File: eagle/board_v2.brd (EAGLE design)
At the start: 104.4 x 80.6 mm, 35 parts, among them J1 RJ11-4X, J2 RJ11-4X, Q1 BD140, Q10 BD140, Q11 BD140, Q12 BD140, Q13 BD140, Q14 BD140, Q15 BD140, Q2 BD140, Q3 BD140, Q4 BD140, Q5 BD140, Q6 BD140, Q7 BD140, Q8 BD140, Q9 BD140, X1 RJ45-8X, X2 RJ45-8X, X3 RJ45-8X, X4 RJ45-8X, X5 RJ45-8X, X6 RJ45-8X

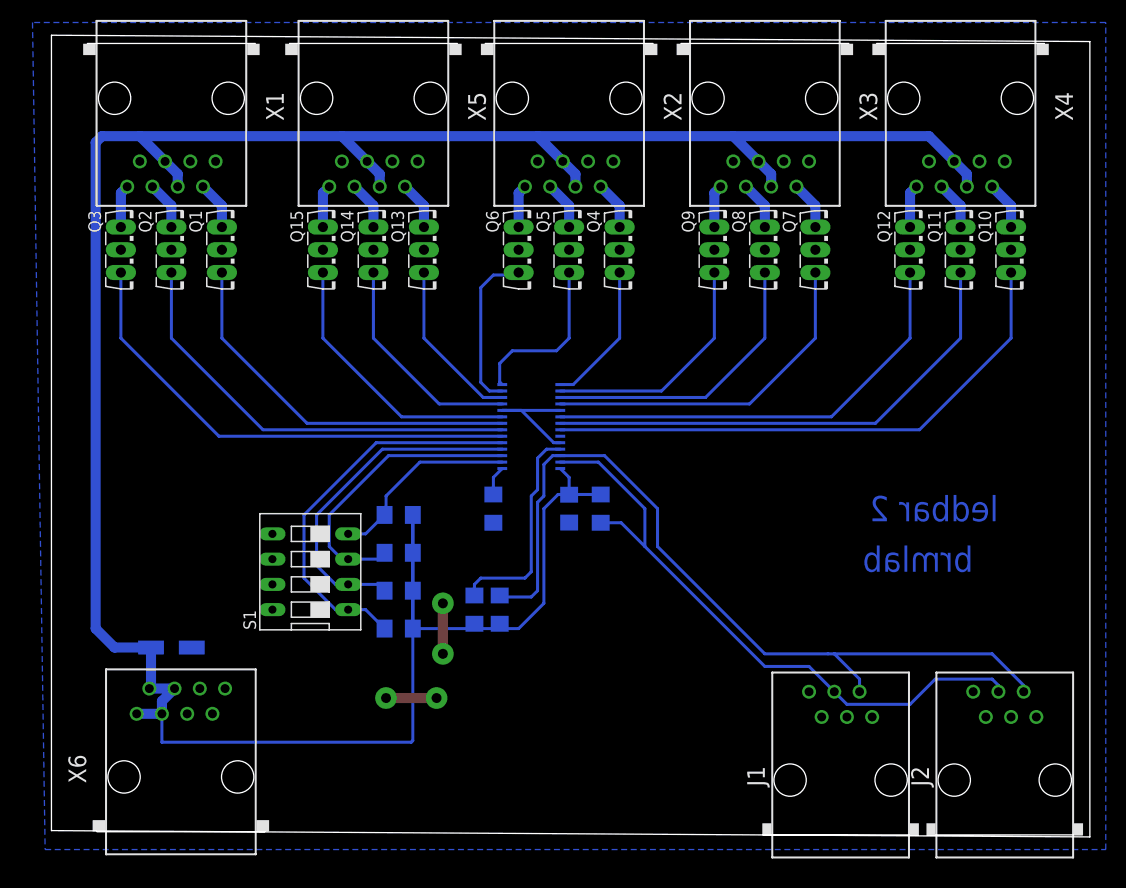
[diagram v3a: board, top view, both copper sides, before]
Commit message: i2c in crossover; removed jumper wires
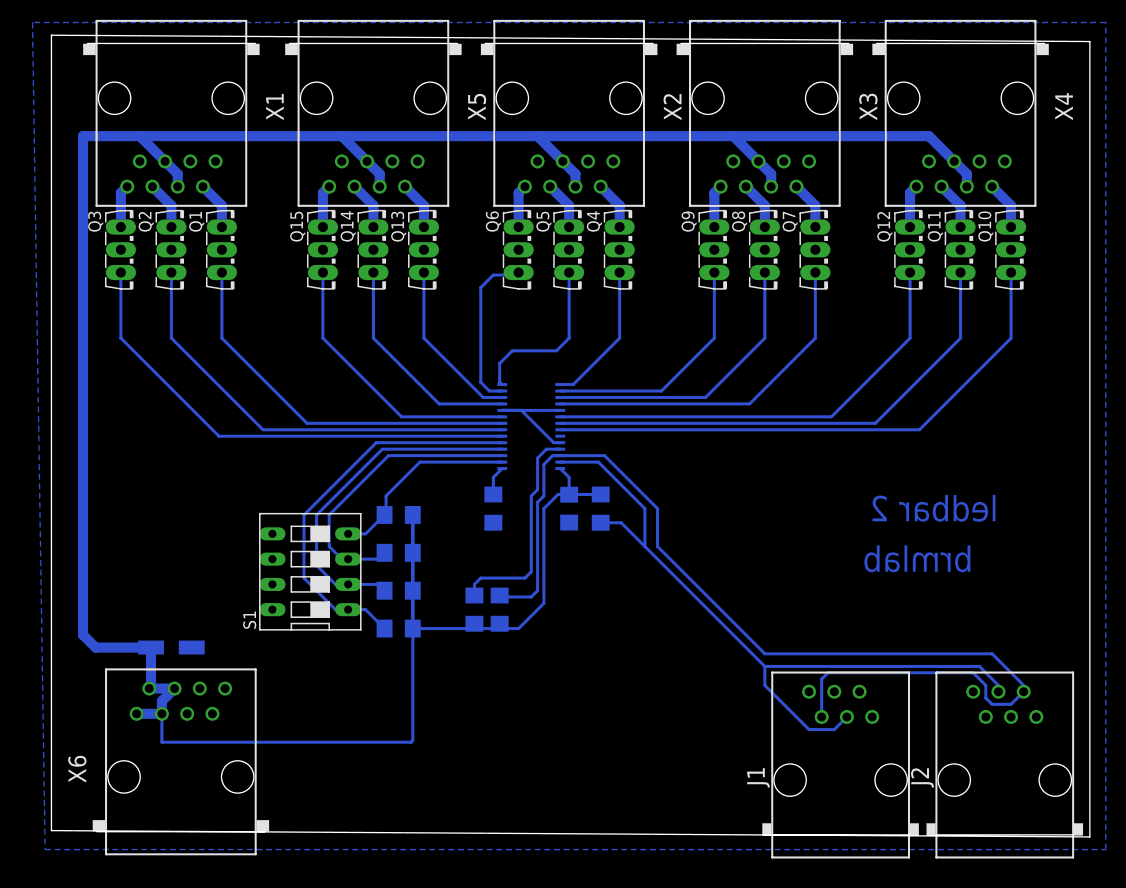
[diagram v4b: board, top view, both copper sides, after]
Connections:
- net GND: now also J1.3, J1.5; no longer J1.2, J1.4
- net N$37: now also J1.2; no longer J1.5
- net N$38: now also J1.4; no longer J1.3
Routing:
- net N$37: track 83.0 -> 105.1 mm
- net N$38: track 63.8 -> 74.2 mm
- net GND: track 23.2 -> 13.0 mm, vias 4 -> 0
- net +5V: track 284.5 -> 287.8 mm
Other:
- board text added: "C1"
- board text added: "C2"
- board text added: "J1"
- board text added: "J2"
- board text added: "Q1"
- board text added: "Q10"
- board text added: "Q11"
- board text added: "Q12"
- board text added: "Q13"
- board text added: "Q14"
- board text added: "Q15"
- board text added: "Q2"
- board text added: "Q3"
- board text added: "Q4"
- board text added: "Q5"
- board text added: "Q6"
- board text added: "Q7"
- board text added: "Q8"
- board text added: "Q9"
- board text added: "R1"
- board text added: "R2"
- board text added: "R3"
- board text added: "R4"
- board text added: "R5"
- board text added: "R6"
- board text added: "R7"
- board text added: "R8"
- board text added: "S1"
- board text added: "U$1"
- board text added: "X1"
- board text added: "X2"
- board text added: "X3"
- board text added: "X4"
- board text added: "X5"
- board text added: "X6"
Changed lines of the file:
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@@
 <layer number="97" name="Info" color="7" fill="1" visible="no" active="no"/>
 <layer number="98" name="Guide" color="6" fill="1" visible="no" active="no"/>
+<layer number="125" name="_tNames" color="14" fill="1" visible="yes" active="yes"/>
+<layer number="126" name="_bNames" color="5" fill="1" visible="yes" active="yes"/>
 <layer number="250" name="Descript" color="3" fill="1" visible="no" active="no"/>
 <layer number="251" name="SMDround" color="12" fill="11" visible="no" active="no"/>
@@
 <text x="95.25" y="31.115" size="2.54" layer="16" font="vector" rot="MR0">ledbar 2</text>
 <text x="92.71" y="26.035" size="2.54" layer="16" font="vector" rot="MR0">brmlab</text>
+<text x="50.927" y="33.655" size="1.27" layer="126" rot="MR270">C1</text>
+<text x="14.66499375" y="21.16500625" size="1.016" layer="126" rot="MR0">C2</text>
+<text x="71.755" y="4.445" size="1.778" layer="125" rot="R90">J1</text>
+<text x="88.265" y="4.445" size="1.778" layer="125" rot="R90">J2</text>
+<text x="13.8684" y="62.3824" size="1.27" layer="125" ratio="10" rot="R270">Q1</text>
+<text x="8.7884" y="62.3824" size="1.27" layer="125" ratio="10" rot="R270">Q2</text>
+<text x="3.7084" y="62.3824" size="1.27" layer="125" ratio="10" rot="R270">Q3</text>
+<text x="53.8734" y="62.3824" size="1.27" layer="125" ratio="10" rot="R270">Q4</text>
+<text x="48.7934" y="62.3824" size="1.27" layer="125" ratio="10" rot="R270">Q5</text>
+<text x="43.7134" y="62.3824" size="1.27" layer="125" ratio="10" rot="R270">Q6</text>
+<text x="73.5584" y="62.3824" size="1.27" layer="125" ratio="10" rot="R270">Q7</text>
+<text x="68.4784" y="62.3824" size="1.27" layer="125" ratio="10" rot="R270">Q8</text>
+<text x="63.3984" y="62.3824" size="1.27" layer="125" ratio="10" rot="R270">Q9</text>
+<text x="93.2434" y="62.3824" size="1.27" layer="125" ratio="10" rot="R270">Q10</text>
+<text x="88.1634" y="62.3824" size="1.27" layer="125" ratio="10" rot="R270">Q11</text>
+<text x="83.0834" y="62.3824" size="1.27" layer="125" ratio="10" rot="R270">Q12</text>
+<text x="34.1884" y="62.3824" size="1.27" layer="125" ratio="10" rot="R270">Q13</text>
+<text x="29.1084" y="62.3824" size="1.27" layer="125" ratio="10" rot="R270">Q14</text>
+<text x="24.0284" y="62.3824" size="1.27" layer="125" ratio="10" rot="R270">Q15</text>
+<text x="45.593" y="30.988" size="1.27" layer="126" rot="MR90">R1</text>
+<text x="43.942" y="23.622" size="1.27" layer="126" rot="MR270">R2</text>
+<text x="56.388" y="30.988" size="1.27" layer="126" rot="MR90">R3</text>
+<text x="41.402" y="23.622" size="1.27" layer="126" rot="MR270">R4</text>
+<text x="36.322" y="21.463" size="1.27" layer="126" rot="MR0">R5</text>
+<text x="36.322" y="25.273" size="1.27" layer="126" rot="MR0">R6</text>
+<text x="36.322" y="29.083" size="1.27" layer="126" rot="MR0">R7</text>
+<text x="36.322" y="32.893" size="1.27" layer="126" rot="MR0">R8</text>
+<text x="20.574" y="20.193" size="1.27" layer="125" ratio="10" rot="R90">S1</text>
+<text x="46.1772" y="35.469396875" size="1.016" layer="126" ratio="10" rot="MR180">U$1</text>
+<text x="21.59" y="74.295" size="1.778" layer="125" rot="R270">X1</text>
+<text x="61.595" y="74.295" size="1.778" layer="125" rot="R270">X2</text>
+<text x="81.28" y="74.295" size="1.778" layer="125" rot="R270">X3</text>
+<text x="100.965" y="74.295" size="1.778" layer="125" rot="R270">X4</text>
+<text x="41.91" y="74.295" size="1.778" layer="125" rot="R270">X5</text>
+<text x="3.4925" y="4.7625" size="1.778" layer="125" rot="R90">X6</text>
 </plain>
 <attributes>
@@
 <param name="mtCopper" value="0.035mm 0.035mm 0.035mm 0.035mm 0.035mm 0.035mm 0.035mm 0.035mm 0.035mm 0.035mm 0.035mm 0.035mm 0.035mm 0.035mm 0.035mm 0.035mm"/>
 <param name="mtIsolate" value="1.5mm 0.15mm 0.2mm 0.15mm 0.2mm 0.15mm 0.2mm 0.15mm 0.2mm 0.15mm 0.2mm 0.15mm 0.2mm 0.15mm 0.2mm"/>
-<param name="mdWireWire" value="16mil"/>
+<param name="mdWireWire" value="20mil"/>
 <param name="mdWirePad" value="20mil"/>
-<param name="mdWireVia" value="16mil"/>
-<param name="mdPadPad" value="16mil"/>
-<param name="mdPadVia" value="16mil"/>
-<param name="mdViaVia" value="16mil"/>
+<param name="mdWireVia" value="20mil"/>
+<param name="mdPadPad" value="20mil"/>
+<param name="mdPadVia" value="20mil"/>
+<param name="mdViaVia" value="20mil"/>
 <param name="mdSmdPad" value="0mil"/>
 <param name="mdSmdVia" value="0mil"/>
@@
 <wire x1="48.895" y1="69.85" x2="29.21" y2="69.85" width="1.016" layer="16"/>
 <wire x1="29.21" y1="69.85" x2="8.89" y2="69.85" width="1.016" layer="16"/>
-<wire x1="8.89" y1="69.85" x2="5.08" y2="69.85" width="1.016" layer="16"/>
-<wire x1="5.08" y1="69.85" x2="4.445" y2="69.215" width="1.016" layer="16"/>
-<wire x1="4.445" y1="69.215" x2="4.445" y2="20.32" width="1.016" layer="16"/>
-<wire x1="4.445" y1="20.32" x2="6.35" y2="18.415" width="1.016" layer="16"/>
-<wire x1="6.35" y1="18.415" x2="10.015" y2="18.415" width="1.016" layer="16"/>
+<wire x1="8.89" y1="69.85" x2="3.175" y2="69.85" width="1.016" layer="16"/>
+<wire x1="3.175" y1="69.85" x2="3.175" y2="19.685" width="1.016" layer="16"/>
+<wire x1="3.175" y1="19.685" x2="4.445" y2="18.415" width="1.016" layer="16"/>
+<wire x1="4.445" y1="18.415" x2="10.015" y2="18.415" width="1.016" layer="16"/>
 <wire x1="55.245" y1="33.807" x2="52.092" y2="33.807" width="0.3048" layer="16"/>
 <wire x1="52.092" y1="33.807" x2="52.07" y2="33.785" width="0.3048" layer="16"/>
@@
 <wire x1="45.3422" y1="42.265" x2="47.27" y2="42.265" width="0.3048" layer="16"/>
 <wire x1="45.3422" y1="42.265" x2="51.1778" y2="42.265" width="0.3048" layer="16"/>
-<via x="39.37" y="17.78" extent="1-16" drill="1" diameter="2.1844"/>
-<via x="39.37" y="22.86" extent="1-16" drill="1" diameter="2.1844"/>
-<wire x1="39.37" y1="22.86" x2="39.37" y2="17.78" width="1.016" layer="1"/>
-<via x="33.655" y="13.335" extent="1-16" drill="1" diameter="2.1844"/>
-<via x="38.735" y="13.335" extent="1-16" drill="1" diameter="2.1844"/>
-<wire x1="33.655" y1="13.335" x2="38.735" y2="13.335" width="1.016" layer="1"/>
-<contactref element="J1" pad="4"/>
-<contactref element="J1" pad="2"/>
 <contactref element="J2" pad="4"/>
 <contactref element="J2" pad="2"/>
@@
 <contactref element="X6" pad="7"/>
 <contactref element="X6" pad="5"/>
+<contactref element="J1" pad="3"/>
+<contactref element="J1" pad="5"/>
 </signal>
 <signal name="N$4">
@@
 <wire x1="48.26" y1="23.495" x2="45.237" y2="23.495" width="0.3048" layer="16"/>
 <wire x1="45.237" y1="23.495" x2="45.085" y2="23.647" width="0.3048" layer="16"/>
-<contactref element="J1" pad="5"/>
-<wire x1="71.755" y1="17.78" x2="78.105" y2="17.78" width="0.3048" layer="16"/>
-<wire x1="78.105" y1="17.78" x2="78.74" y2="17.78" width="0.3048" layer="16"/>
-<wire x1="78.74" y1="17.78" x2="81.28" y2="15.24" width="0.3048" layer="16"/>
-<wire x1="81.28" y1="15.24" x2="81.28" y2="13.97" width="0.3048" layer="16"/>
 <contactref element="J2" pad="5"/>
 <wire x1="97.79" y1="13.97" x2="97.79" y2="14.605" width="0.3048" layer="16"/>
 <wire x1="97.79" y1="14.605" x2="94.615" y2="17.78" width="0.3048" layer="16"/>
-<wire x1="94.615" y1="17.78" x2="78.74" y2="17.78" width="0.3048" layer="16"/>
+<wire x1="94.615" y1="17.78" x2="71.755" y2="17.78" width="0.3048" layer="16"/>
+<contactref element="J1" pad="2"/>
+<wire x1="77.47" y1="11.43" x2="77.47" y2="15.24" width="0.3048" layer="16"/>
+<wire x1="77.47" y1="15.24" x2="78.105" y2="15.875" width="0.3048" layer="16"/>
+<wire x1="78.105" y1="15.875" x2="92.71" y2="15.875" width="0.3048" layer="16"/>
+<wire x1="92.71" y1="15.875" x2="93.98" y2="14.605" width="0.3048" layer="16"/>
+<wire x1="93.98" y1="14.605" x2="93.98" y2="13.335" width="0.3048" layer="16"/>
+<wire x1="93.98" y1="13.335" x2="94.615" y2="12.7" width="0.3048" layer="16"/>
+<wire x1="94.615" y1="12.7" x2="96.52" y2="12.7" width="0.3048" layer="16"/>
+<wire x1="96.52" y1="12.7" x2="97.79" y2="13.97" width="0.3048" layer="16"/>
 </signal>
 <signal name="N$38">
@@
 <wire x1="55.01" y1="37.065" x2="59.69" y2="32.385" width="0.3048" layer="16"/>
 <wire x1="59.69" y1="32.385" x2="59.69" y2="28.575" width="0.3048" layer="16"/>
-<wire x1="59.69" y1="28.575" x2="71.755" y2="16.51" width="0.3048" layer="16"/>
 <wire x1="55.245" y1="30.963" x2="57.302" y2="30.963" width="0.3048" layer="16"/>
 <wire x1="57.302" y1="30.963" x2="59.69" y2="28.575" width="0.3048" layer="16"/>
-<contactref element="J1" pad="3"/>
-<wire x1="71.755" y1="16.51" x2="76.2" y2="16.51" width="0.3048" layer="16"/>
-<wire x1="76.2" y1="16.51" x2="78.74" y2="13.97" width="0.3048" layer="16"/>
 <contactref element="J2" pad="3"/>
 <wire x1="95.25" y1="13.97" x2="95.25" y2="14.605" width="0.3048" layer="16"/>
-<wire x1="95.25" y1="14.605" x2="94.615" y2="15.24" width="0.3048" layer="16"/>
-<wire x1="94.615" y1="15.24" x2="88.9" y2="15.24" width="0.3048" layer="16"/>
-<wire x1="88.9" y1="15.24" x2="86.36" y2="12.7" width="0.3048" layer="16"/>
-<wire x1="86.36" y1="12.7" x2="80.01" y2="12.7" width="0.3048" layer="16"/>
-<wire x1="80.01" y1="12.7" x2="78.74" y2="13.97" width="0.3048" layer="16"/>
+<contactref element="J1" pad="4"/>
+<wire x1="59.69" y1="28.575" x2="71.755" y2="16.51" width="0.3048" layer="16"/>
+<wire x1="71.755" y1="16.51" x2="93.345" y2="16.51" width="0.3048" layer="16"/>
+<wire x1="93.345" y1="16.51" x2="95.25" y2="14.605" width="0.3048" layer="16"/>
+<wire x1="80.01" y1="11.43" x2="78.74" y2="10.16" width="0.3048" layer="16"/>
+<wire x1="78.74" y1="10.16" x2="76.2" y2="10.16" width="0.3048" layer="16"/>
+<wire x1="76.2" y1="10.16" x2="71.755" y2="14.605" width="0.3048" layer="16"/>
+<wire x1="71.755" y1="14.605" x2="71.755" y2="16.51" width="0.3048" layer="16"/>
 </signal>
 <signal name="N$17">

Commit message: board v2.1
  * PCB size has been optimized
  * Layout has been redesigned to minimize current loop area.
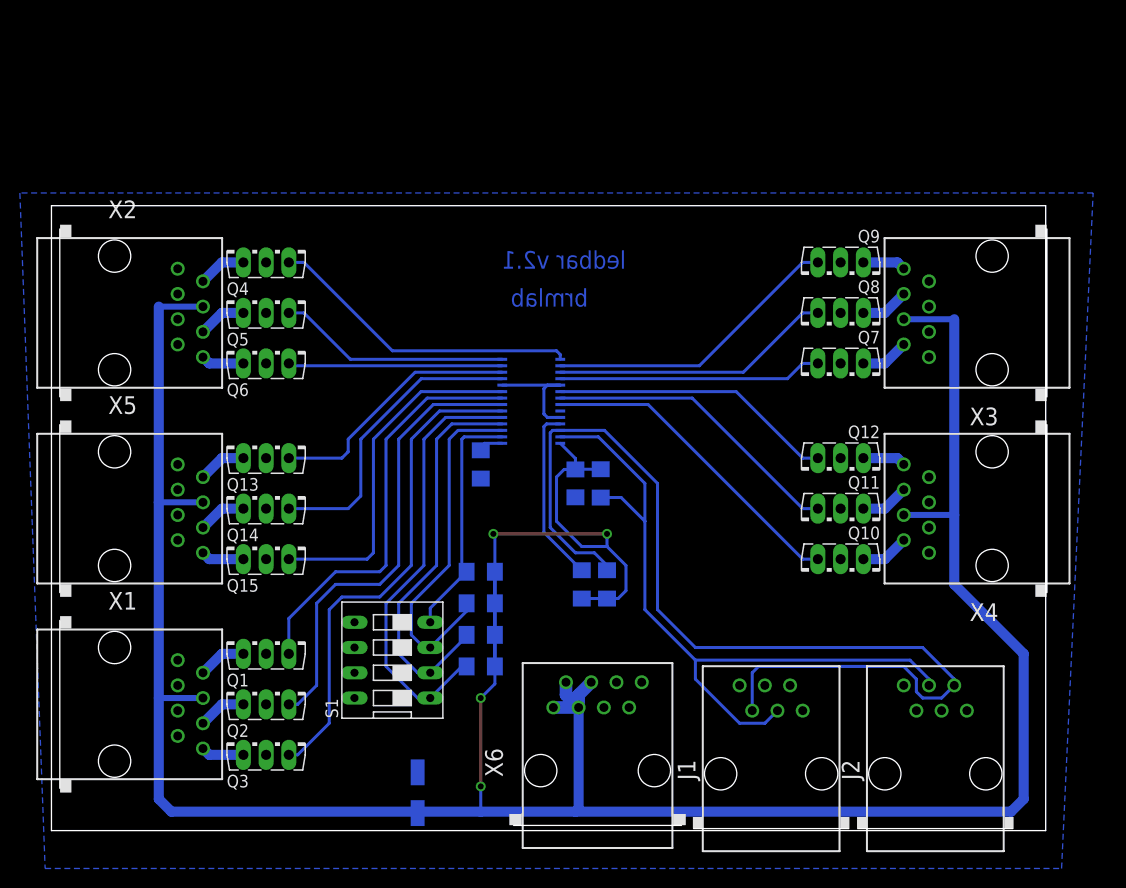
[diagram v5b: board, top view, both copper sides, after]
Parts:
- moved X1 61.2 mm to (6.35, 12.7), turned to 270 degrees
- moved Q3 51.3 mm to (21.6, 8.89), turned to 0 degrees
- moved X2 50.6 mm to (6.35, 52.1), turned to 270 degrees
- moved X5 48.8 mm to (6.35, 32.4), turned to 270 degrees
- moved Q2 45.2 mm to (21.6, 14.0), turned to 0 degrees
- moved X6 41.9 mm to (54.9, 6.03)
- moved X4 41.4 mm to (94.6, 32.4), turned to 90 degrees
- moved Q1 39.5 mm to (21.6, 19.1), turned to 0 degrees
- moved Q10 37.3 mm to (79.4, 26.0), turned to 180 degrees
- moved Q4 36.8 mm to (21.6, 58.4), turned to 0 degrees
- moved Q5 32.2 mm to (21.6, 53.3), turned to 0 degrees
- moved X3 31.4 mm to (94.6, 52.1), turned to 90 degrees
- moved Q15 30.7 mm to (21.6, 28.6), turned to 0 degrees
- moved Q11 30.4 mm to (79.4, 31.1), turned to 180 degrees
- moved C2 28.8 mm to (36.8, 3.81), turned to 270 degrees
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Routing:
- net +5V: track 287.8 -> 312.3 mm, vias 0 -> 4
- net N$35: track 55.8 -> 32.4 mm
- net N$34: track 50.4 -> 30.5 mm
- net N$29: track 14.5 -> 31.6 mm
- net N$33: track 45.1 -> 28.7 mm
- net N$26: track 17.0 -> 25.8 mm
- net N$32: track 35.0 -> 26.5 mm
- net N$25: track 22.3 -> 30.2 mm
- net N$16: track 27.9 -> 35.1 mm
- net N$28: track 16.9 -> 23.4 mm
- net N$18: track 29.4 -> 35.4 mm
- net N$30: track 24.3 -> 30.2 mm
- net N$19: track 34.4 -> 39.7 mm
- net N$17: track 19.5 -> 24.8 mm
- net N$27: track 16.5 -> 21.6 mm
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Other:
- board size 104.4 x 80.6 mm -> 100 x 62.9 mm
- board text added: "ledbar v2.1"
- board text removed: "X1"
- board text removed: "X5"
- board text removed: "ledbar 2"
